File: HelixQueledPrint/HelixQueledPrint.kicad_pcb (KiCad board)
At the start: 2 copper layers, 4 parts, among them U201 TPS92201, U301 TPS92201, U401 TPS92201, U501 TPS92201

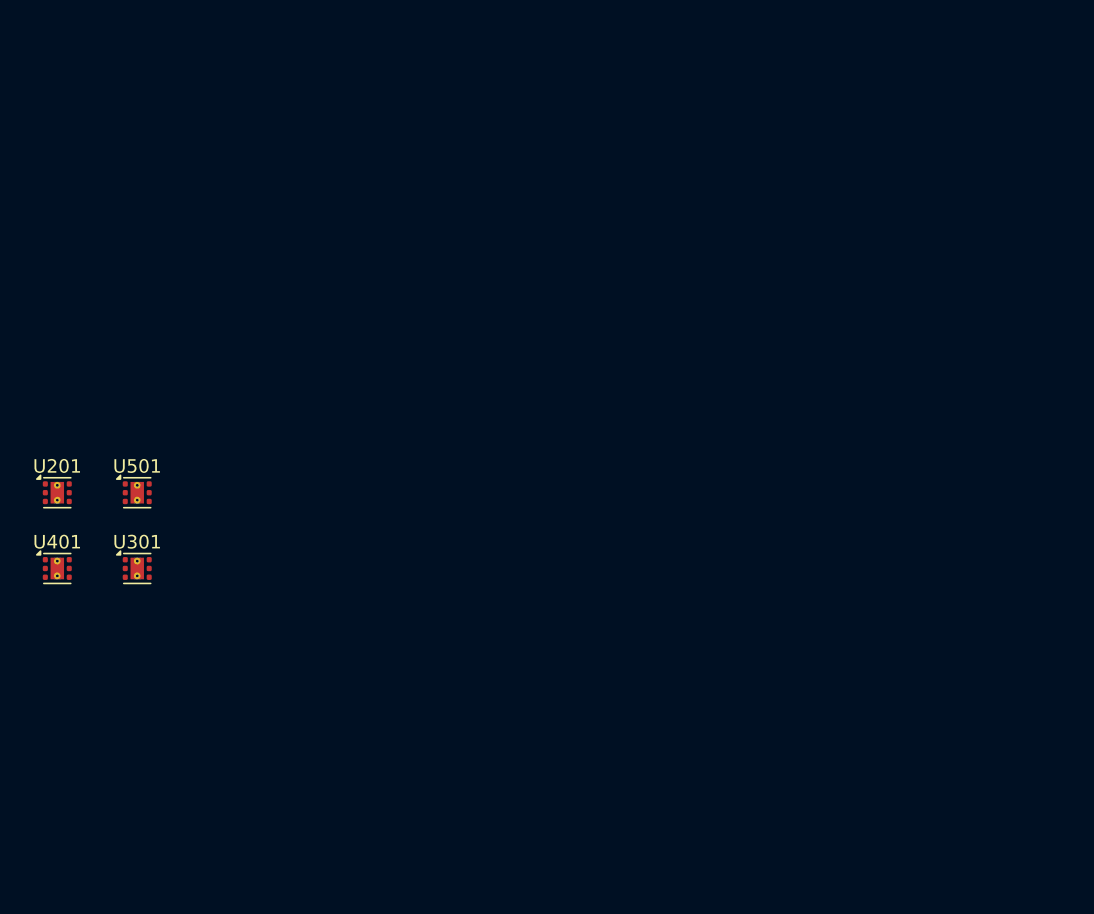
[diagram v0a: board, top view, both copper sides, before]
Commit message: Netklases toegevoegd, componenten naar pcb geplaatst
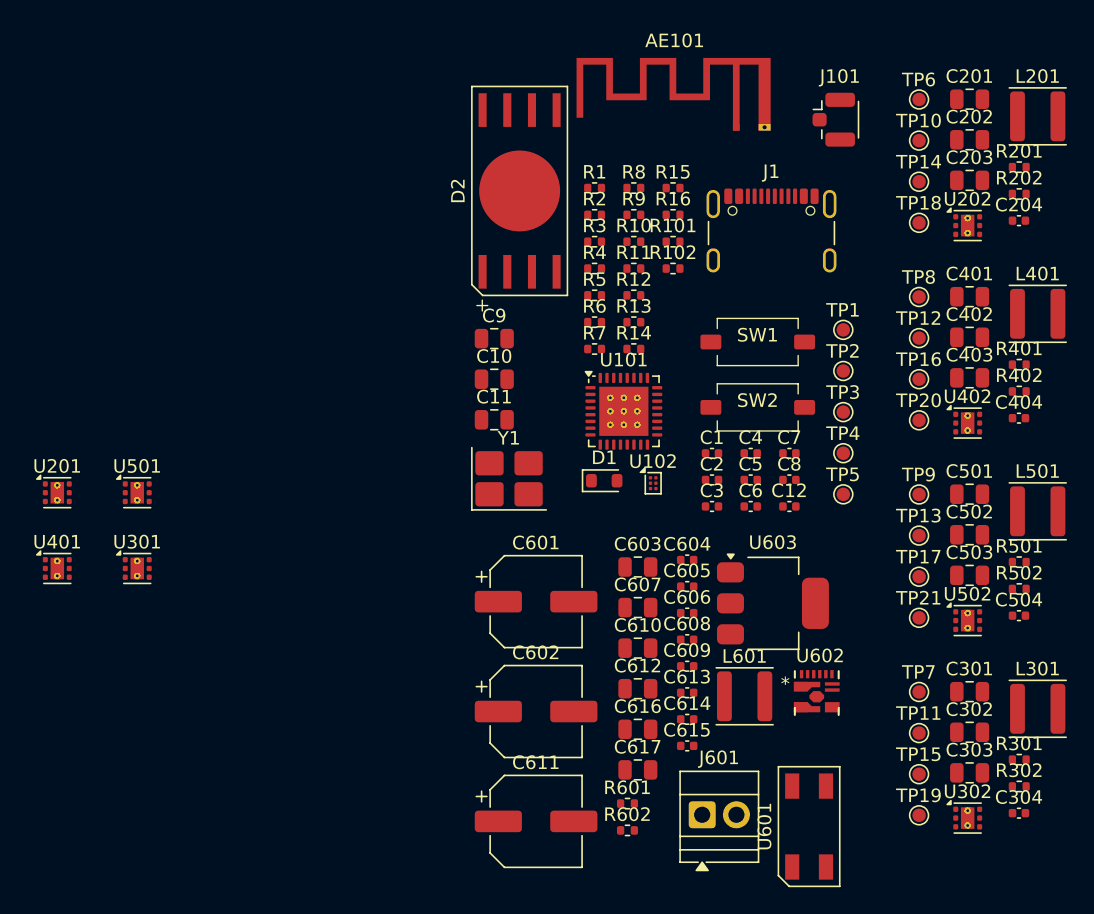
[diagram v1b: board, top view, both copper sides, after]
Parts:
- added AE101: Antenna_Shield, RF_Antenna:Texas_SWRA117D_2.4GHz_Left, F.Cu at (176.6, 50.6)
- added C1: 18pF 50V, Capacitor_SMD:C_0402_1005Metric, F.Cu at (174.8, 74.8)
- added C10: 10uF 25V, Capacitor_SMD:C_0805_2012Metric, F.Cu at (158.6, 69.3)
- added C11: 10uF 25V, Capacitor_SMD:C_0805_2012Metric, F.Cu at (158.6, 72.3)
- added C12: 100nF 25V, Capacitor_SMD:C_0402_1005Metric, F.Cu at (180.5, 78.8)
- added C2: 18pF 50V, Capacitor_SMD:C_0402_1005Metric, F.Cu at (174.8, 76.8)
- added C201: 10uF 25V, Capacitor_SMD:C_0805_2012Metric, F.Cu at (193.9, 48.5)
- added C202: 10uF 25V, Capacitor_SMD:C_0805_2012Metric, F.Cu at (193.9, 51.5)
- added C203: 10uF 25V, Capacitor_SMD:C_0805_2012Metric, F.Cu at (193.9, 54.6)
- added C204: 100nF 25V, Capacitor_SMD:C_0402_1005Metric, F.Cu at (197.5, 57.5)
- added C3: 100nF 25V, Capacitor_SMD:C_0402_1005Metric, F.Cu at (174.8, 78.8)
- added C301: 10uF 25V, Capacitor_SMD:C_0805_2012Metric, F.Cu at (193.9, 92.5)
- added C302: 10uF 25V, Capacitor_SMD:C_0805_2012Metric, F.Cu at (193.9, 95.5)
- added C303: 10uF 25V, Capacitor_SMD:C_0805_2012Metric, F.Cu at (193.9, 98.5)
- added C304: 100nF 25V, Capacitor_SMD:C_0402_1005Metric, F.Cu at (197.5, 101.5)
- added C4: 100nF 25V, Capacitor_SMD:C_0402_1005Metric, F.Cu at (177.6, 74.8)
- added C401: 10uF 25V, Capacitor_SMD:C_0805_2012Metric, F.Cu at (193.9, 63.2)
- added C402: 10uF 25V, Capacitor_SMD:C_0805_2012Metric, F.Cu at (193.9, 66.2)
- added C403: 10uF 25V, Capacitor_SMD:C_0805_2012Metric, F.Cu at (193.9, 69.2)
- added C404: 100nF 25V, Capacitor_SMD:C_0402_1005Metric, F.Cu at (197.5, 72.2)
- added C5: 100nF 25V, Capacitor_SMD:C_0402_1005Metric, F.Cu at (177.6, 76.8)
- added C501: 10uF 25V, Capacitor_SMD:C_0805_2012Metric, F.Cu at (193.9, 77.8)
- added C502: 10uF 25V, Capacitor_SMD:C_0805_2012Metric, F.Cu at (193.9, 80.8)
- added C503: 10uF 25V, Capacitor_SMD:C_0805_2012Metric, F.Cu at (193.9, 83.9)
- added C504: 100nF 25V, Capacitor_SMD:C_0402_1005Metric, F.Cu at (197.5, 86.8)
- added C6: 100nF 25V, Capacitor_SMD:C_0402_1005Metric, F.Cu at (177.6, 78.8)
- added C601: 68uF 25V, Capacitor_SMD:CP_Elec_6.3x5.4, F.Cu at (161.7, 85.8)
- added C602: 68uF 25V, Capacitor_SMD:CP_Elec_6.3x5.4, F.Cu at (161.7, 94.0)
- added C603: 10uF 25V, Capacitor_SMD:C_0805_2012Metric, F.Cu at (169.2, 83.2)
- added C604: 100nF 25V, Capacitor_SMD:C_0402_1005Metric, F.Cu at (172.9, 82.7)
- added C605: 100nF 25V, Capacitor_SMD:C_0402_1005Metric, F.Cu at (172.9, 84.7)
- added C606: 100nF 25V, Capacitor_SMD:C_0402_1005Metric, F.Cu at (172.9, 86.7)
- added C607: 10uF 25V, Capacitor_SMD:C_0805_2012Metric, F.Cu at (169.2, 86.2)
- added C608: 100nF 25V, Capacitor_SMD:C_0402_1005Metric, F.Cu at (172.9, 88.6)
- added C609: 100nF 25V, Capacitor_SMD:C_0402_1005Metric, F.Cu at (172.9, 90.6)
- added C610: 10uF 25V, Capacitor_SMD:C_0805_2012Metric, F.Cu at (169.2, 89.3)
- added C611: 68uF 25V, Capacitor_SMD:CP_Elec_6.3x5.4, F.Cu at (161.7, 102.1)
- added C612: 10uF 25V, Capacitor_SMD:C_0805_2012Metric, F.Cu at (169.2, 92.3)
- added C613: 100nF 25V, Capacitor_SMD:C_0402_1005Metric, F.Cu at (172.9, 92.6)
- added C614: 100nF 25V, Capacitor_SMD:C_0402_1005Metric, F.Cu at (172.9, 94.5)
- added C615: 100nF 25V, Capacitor_SMD:C_0402_1005Metric, F.Cu at (172.9, 96.5)
- added C616: 10uF 25V, Capacitor_SMD:C_0805_2012Metric, F.Cu at (169.2, 95.3)
- added C617: 10uF 25V, Capacitor_SMD:C_0805_2012Metric, F.Cu at (169.2, 98.3)
- added C7: 100nF 25V, Capacitor_SMD:C_0402_1005Metric, F.Cu at (180.5, 74.8)
- added C8: 100nF 25V, Capacitor_SMD:C_0402_1005Metric, F.Cu at (180.5, 76.8)
- added C9: 10uF 25V, Capacitor_SMD:C_0805_2012Metric, F.Cu at (158.6, 66.3)
- added D1: D_Schottky, Diode_SMD:D_SOD-110, F.Cu at (166.8, 76.8)
- added D2: LED_RGBW, 1CustomFootprints:QR4xLED, F.Cu at (160.5, 55.3)
- added J1: USB_C_Receptacle_USB2.0_16P, Connector_USB:USB_C_Receptacle_GCT_USB4105-xx-A_16P_TopMnt_Horizontal, F.Cu at (179.2, 59.4)
- added J101: Conn_Coaxial, Connector_Coaxial:U.FL_Hirose_U.FL-R-SMT-1_Vertical, F.Cu at (183.8, 50.1)
- added J601: Screw_Terminal_01x02, TerminalBlock:TerminalBlock_Xinya_XY308-2.54-2P_1x02_P2.54mm_Horizontal, F.Cu at (174.0, 101.6)
- added L201: 2.2u, Inductor_SMD:L_APV_ANR4020, F.Cu at (198.9, 49.8)
- added L301: 2.2u, Inductor_SMD:L_APV_ANR4020, F.Cu at (198.9, 93.8)
- added L401: 2.2u, Inductor_SMD:L_APV_ANR4020, F.Cu at (198.9, 64.5)
- added L501: 2.2u, Inductor_SMD:L_APV_ANR4020, F.Cu at (198.9, 79.1)
- added L601: 1.2uH, Inductor_SMD:L_APV_ANR4012, F.Cu at (177.2, 92.8)
- added R1: 10K, Resistor_SMD:R_0402_1005Metric, F.Cu at (166.0, 55.1)
- added R10: 10K, Resistor_SMD:R_0402_1005Metric, F.Cu at (168.9, 59.1)
- added R101: 0R, Resistor_SMD:R_0402_1005Metric, F.Cu at (171.9, 59.1)
- added R102: 0R, Resistor_SMD:R_0402_1005Metric, F.Cu at (171.9, 61.1)
- added R11: 10K, Resistor_SMD:R_0402_1005Metric, F.Cu at (168.9, 61.1)
- added R12: 68K, Resistor_SMD:R_0402_1005Metric, F.Cu at (168.9, 63.1)
- added R13: 68K, Resistor_SMD:R_0402_1005Metric, F.Cu at (168.9, 65.1)
- added R14: 10K, Resistor_SMD:R_0402_1005Metric, F.Cu at (168.9, 67.1)
- added R15: 68K, Resistor_SMD:R_0402_1005Metric, F.Cu at (171.9, 55.1)
- added R16: 10K, Resistor_SMD:R_0402_1005Metric, F.Cu at (171.9, 57.1)
- added R2: 10K, Resistor_SMD:R_0402_1005Metric, F.Cu at (166.0, 57.1)
- added R201: 100m, Resistor_SMD:R_0402_1005Metric, F.Cu at (197.5, 53.6)
- added R202: 10K, Resistor_SMD:R_0402_1005Metric, F.Cu at (197.5, 55.6)
- added R3: 10K, Resistor_SMD:R_0402_1005Metric, F.Cu at (166.0, 59.1)
- added R301: 100m, Resistor_SMD:R_0402_1005Metric, F.Cu at (197.5, 97.5)
- added R302: 10K, Resistor_SMD:R_0402_1005Metric, F.Cu at (197.5, 99.5)
- added R4: 10K, Resistor_SMD:R_0402_1005Metric, F.Cu at (166.0, 61.1)
- added R401: 100m, Resistor_SMD:R_0402_1005Metric, F.Cu at (197.5, 68.2)
- added R402: 10K, Resistor_SMD:R_0402_1005Metric, F.Cu at (197.5, 70.2)
- added R5: 1K2, Resistor_SMD:R_0402_1005Metric, F.Cu at (166.0, 63.1)
- added R501: 100m, Resistor_SMD:R_0402_1005Metric, F.Cu at (197.5, 82.9)
- added R502: 10K, Resistor_SMD:R_0402_1005Metric, F.Cu at (197.5, 84.9)
- added R6: 10K, Resistor_SMD:R_0402_1005Metric, F.Cu at (166.0, 65.1)
- added R601: 68K, Resistor_SMD:R_0402_1005Metric, F.Cu at (168.5, 100.8)
- added R602: 8.2K, Resistor_SMD:R_0402_1005Metric, F.Cu at (168.5, 102.8)
- added R7: 10K, Resistor_SMD:R_0402_1005Metric, F.Cu at (166.0, 67.1)
- added R8: 10K, Resistor_SMD:R_0402_1005Metric, F.Cu at (168.9, 55.1)
- added R9: 10K, Resistor_SMD:R_0402_1005Metric, F.Cu at (168.9, 57.1)
- added SW1: SW_SPST, 1CustomFootprints:TS1101A26025, F.Cu at (178.1, 66.5)
- added SW2: SW_SPST, 1CustomFootprints:TS1101A26025, F.Cu at (178.1, 71.4)
- added TP1: TestPoint, TestPoint:TestPoint_Pad_D1.0mm, F.Cu at (184.5, 65.7)
- added TP10: TestPoint, TestPoint:TestPoint_Pad_D1.0mm, F.Cu at (190.1, 51.6)
- added TP11: TestPoint, TestPoint:TestPoint_Pad_D1.0mm, F.Cu at (190.1, 95.6)
- added TP12: TestPoint, TestPoint:TestPoint_Pad_D1.0mm, F.Cu at (190.1, 66.3)
- added TP13: TestPoint, TestPoint:TestPoint_Pad_D1.0mm, F.Cu at (190.1, 80.9)
- added TP14: TestPoint, TestPoint:TestPoint_Pad_D1.0mm, F.Cu at (190.1, 54.7)
- added TP15: TestPoint, TestPoint:TestPoint_Pad_D1.0mm, F.Cu at (190.1, 98.6)
- added TP16: TestPoint, TestPoint:TestPoint_Pad_D1.0mm, F.Cu at (190.1, 69.3)
- added TP17: TestPoint, TestPoint:TestPoint_Pad_D1.0mm, F.Cu at (190.1, 84.0)
- added TP18: TestPoint, TestPoint:TestPoint_Pad_D1.0mm, F.Cu at (190.1, 57.7)
- added TP19: TestPoint, TestPoint:TestPoint_Pad_D1.0mm, F.Cu at (190.1, 101.7)
- added TP2: TestPoint, TestPoint:TestPoint_Pad_D1.0mm, F.Cu at (184.5, 68.7)
- added TP20: TestPoint, TestPoint:TestPoint_Pad_D1.0mm, F.Cu at (190.1, 72.4)
- added TP21: TestPoint, TestPoint:TestPoint_Pad_D1.0mm, F.Cu at (190.1, 87.0)
- added TP3: TestPoint, TestPoint:TestPoint_Pad_D1.0mm, F.Cu at (184.5, 71.8)
- added TP4: TestPoint, TestPoint:TestPoint_Pad_D1.0mm, F.Cu at (184.5, 74.8)
- added TP5: TestPoint, TestPoint:TestPoint_Pad_D1.0mm, F.Cu at (184.5, 77.8)
- added TP6: TestPoint, TestPoint:TestPoint_Pad_D1.0mm, F.Cu at (190.1, 48.6)
- added TP7: TestPoint, TestPoint:TestPoint_Pad_D1.0mm, F.Cu at (190.1, 92.5)
- added TP8: TestPoint, TestPoint:TestPoint_Pad_D1.0mm, F.Cu at (190.1, 63.2)
- added TP9: TestPoint, TestPoint:TestPoint_Pad_D1.0mm, F.Cu at (190.1, 77.9)
- added U101: ESP32-C6FHx, Package_DFN_QFN:QFN-32-1EP_5x5mm_P0.5mm_EP3.65x3.65mm_ThermalVias, F.Cu at (168.2, 71.7)
- added U102: BGS12WN6E6327, Package_LGA:Infineon_PG-TSNP-6-10_0.7x1.1mm_0.7x1.1mm_P0.4mm, F.Cu at (170.4, 77.0)
- added U202: TPS92201, Package_SON:WSON-6-1EP_2x2mm_P0.65mm_EP1x1.6mm_ThermalVias, F.Cu at (193.7, 57.9)
- added U302: TPS92201, Package_SON:WSON-6-1EP_2x2mm_P0.65mm_EP1x1.6mm_ThermalVias, F.Cu at (193.7, 101.9)
- added U402: TPS92201, Package_SON:WSON-6-1EP_2x2mm_P0.65mm_EP1x1.6mm_ThermalVias, F.Cu at (193.7, 72.6)
- added U502: TPS92201, Package_SON:WSON-6-1EP_2x2mm_P0.65mm_EP1x1.6mm_ThermalVias, F.Cu at (193.7, 87.2)
- added U601: MB34F, 1CustomFootprints:MFB, F.Cu at (181.9, 102.5)
- added U602: SY8366H, 1CustomFootprints:QFN3X3-12_SGY, F.Cu at (182.5, 92.6)
- added U603: XBL1117, Package_TO_SOT_SMD:SOT-223, F.Cu at (179.3, 85.9)
- added Y1: 40MHz, Crystal:Crystal_SMD_3225-4Pin_3.2x2.5mm_HandSoldering, F.Cu at (159.7, 76.7)
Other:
- copper layers 2 -> 4
